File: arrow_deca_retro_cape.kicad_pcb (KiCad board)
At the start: 2 copper layers, 100 x 100 mm, 60 parts, among them J1 DB15_Female_HighDensity, J10 Conn_02x06_Odd_Even, J11 PMOD1, J12 PMOD2, J14 Conn_01x02, J15 Conn_01x03, J16 Conn_01x06, J17 Conn_01x02, J18 Conn_01x03, J19 DINC_MIN_TM_6_1, J2 Conn_01x03, J20 PMOD3, J21 USB3_A, J22 Conn_01x03, J3 Conn_01x06, J4 DB9_Male_MountingHoles, J5 DINC_MIN_TM_6_1, J6 Conn_02x20_Odd_Even, J7 Conn_01x03, J8 P8_Male, J9 P9_Male, U4 LM1117-3.3, U5 LM1117-2.5

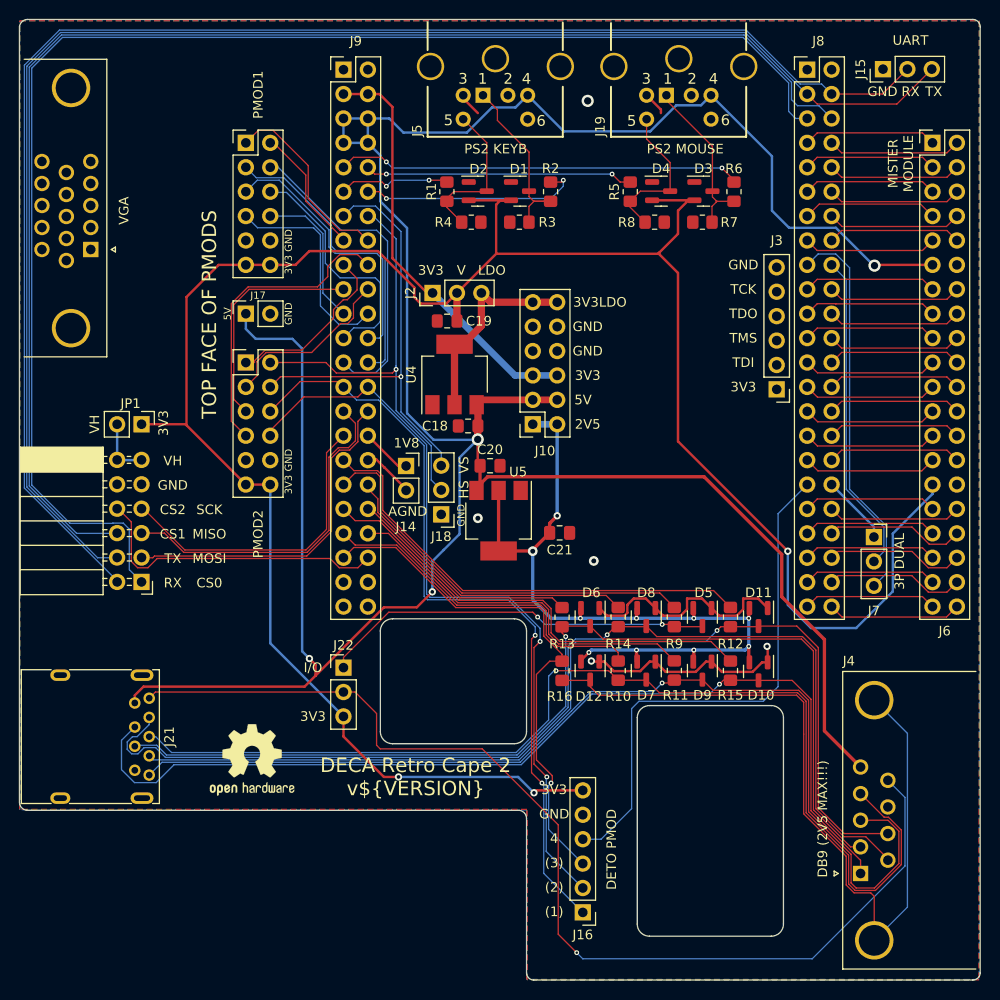
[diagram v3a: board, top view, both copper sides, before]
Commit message: v0.65 power header changed
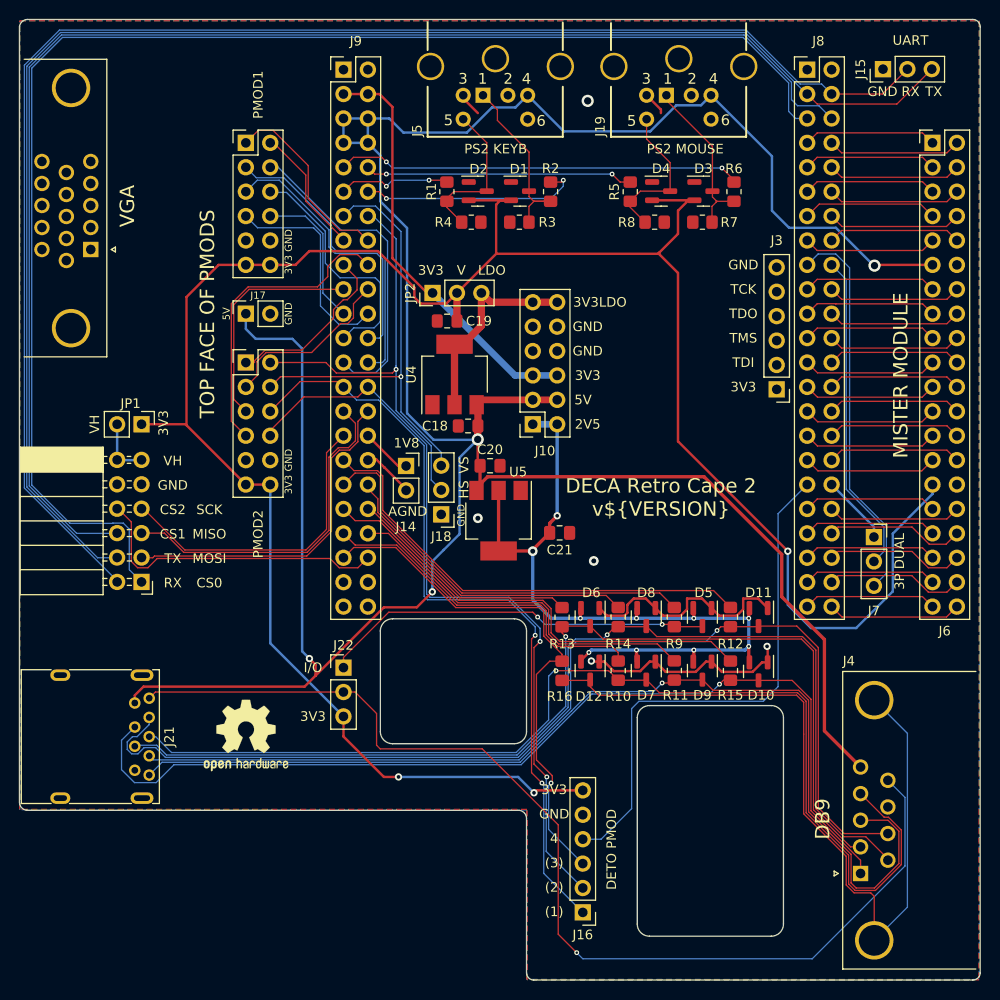
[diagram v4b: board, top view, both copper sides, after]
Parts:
- moved LO2 2.62 mm to (106.7, 114.9)
- renumbered J2 to JP2
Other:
- board text added: "DB9"
- board text removed: "DB9 (2V5 MAX!!!)"
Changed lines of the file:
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@@
     )
   )
-  (property "VERSION" "0.62")
+  (property "VERSION" "0.65")
   (net 0 "")
   (net 1 "GND")
@@
     (property "Sheetname" "")
     (attr through_hole)
-    (fp_text reference "J2" (at 0 -2.33 90) (layer "F.SilkS")
+    (fp_text reference "JP2" (at 0 -2.33 90) (layer "F.SilkS")
       (effects (font (size 1 1) (thickness 0.15)))
     )
@@
   )
   (footprint "Symbol:OSHW-Logo2_9.8x8mm_SilkScreen" (layer "F.Cu")
-    (at 107.315 117.475)
+    (at 106.68 114.935)
     (descr "Open Source Hardware Symbol")
     (tags "Logo Symbol OSHW")
@@
     (effects (font (size 0.75 0.75) (thickness 0.15)))
   )
-  (gr_text "DECA Retro Cape 2\nv${VERSION}" (at 124.333 119.253) (layer "F.SilkS")
+  (gr_text "DECA Retro Cape 2\nv${VERSION}" (at 149.86 90.17) (layer "F.SilkS")
     (effects (font (size 1.5 1.5) (thickness 0.15)))
   )
@@
     (effects (font (size 1 1) (thickness 0.15)))
   )
-  (gr_text "TOP FACE OF PMODS" (at 102.87 71.12 90) (layer "F.SilkS")
+  (gr_text "TOP FACE OF PMODS" (at 102.6668 71.0692 90) (layer "F.SilkS")
     (effects (font (size 1.5 1.5) (thickness 0.15)))
   )
@@
     (effects (font (size 1 1) (thickness 0.15)))
   )
-  (gr_text "DB9 (2V5 MAX!!!)" (at 166.693516 123.623 90) (layer "F.SilkS")
-    (effects (font (size 1 1) (thickness 0.15)))
+  (gr_text "DB9" (at 166.693516 123.623 90) (layer "F.SilkS")
+    (effects (font (size 1.5 1.5) (thickness 0.15)))
   )
   (gr_text "3V3" (at 98.0948 82.423 90) (layer "F.SilkS")
@@
     (effects (font (size 1 1) (thickness 0.15)))
   )
-  (gr_text "MISTER\nMODULE" (at 174.821516 55.424 90) (layer "F.SilkS")
-    (effects (font (size 1 1) (thickness 0.15)))
+  (gr_text "MISTER MODULE" (at 174.821516 77.47 90) (layer "F.SilkS")
+    (effects (font (size 1.5 1.5) (thickness 0.15)))
   )
   (gr_text "VS" (at 129.355516 86.793 90) (layer "F.SilkS")
@@
     (effects (font (size 0.75 0.75) (thickness 0.15)))
   )
-  (gr_text "5V" (at 104.760331 71.045 90) (layer "F.SilkS")
+  (gr_text "5V" (at 104.648 71.045 90) (layer "F.SilkS")
     (effects (font (size 0.75 0.75) (thickness 0.15)))
   )
@@
     (effects (font (size 1 1) (thickness 0.15)))
   )
-  (gr_text "VGA" (at 93.98 60.325 90) (layer "F.SilkS")
-    (effects (font (size 1 1) (thickness 0.15)))
+  (gr_text "VGA" (at 94.3356 59.8424 90) (layer "F.SilkS")
+    (effects (font (size 1.5 1.5) (thickness 0.15)))
   )
   (gr_text "I/O" (at 113.650331 107.875) (layer "F.SilkS")

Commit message: v0.68 vga schematic
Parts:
- added R17: 180, Resistor_SMD:R_0805_2012Metric_Pad1.20x1.40mm_HandSolder, F.Cu at (103.5, 44.5)
- added R18: 180, Resistor_SMD:R_0805_2012Metric_Pad1.20x1.40mm_HandSolder, F.Cu at (103.5, 47.6)
- added R19: 2k, Resistor_SMD:R_0805_2012Metric_Pad1.20x1.40mm_HandSolder, F.Cu at (96.5, 44.5)
- added R20: 2k, Resistor_SMD:R_0805_2012Metric_Pad1.20x1.40mm_HandSolder, F.Cu at (96.5, 46.4)
- added R21: 2k, Resistor_SMD:R_0805_2012Metric_Pad1.20x1.40mm_HandSolder, F.Cu at (96.5, 48.3)
- added R22: 1k, Resistor_SMD:R_0805_2012Metric_Pad1.20x1.40mm_HandSolder, F.Cu at (96.5, 50.2)
- added R23: 1k, Resistor_SMD:R_0805_2012Metric_Pad1.20x1.40mm_HandSolder, F.Cu at (96.5, 52.1)
- added R24: 1k, Resistor_SMD:R_0805_2012Metric_Pad1.20x1.40mm_HandSolder, F.Cu at (96.5, 54.0)
- added R25: 2k, Resistor_SMD:R_0805_2012Metric_Pad1.20x1.40mm_HandSolder, F.Cu at (96.5, 68.6)
- added R26: 2k, Resistor_SMD:R_0805_2012Metric_Pad1.20x1.40mm_HandSolder, F.Cu at (96.5, 70.5)
- added R27: 2k, Resistor_SMD:R_0805_2012Metric_Pad1.20x1.40mm_HandSolder, F.Cu at (96.5, 72.4)
- added R28: 1k, Resistor_SMD:R_0805_2012Metric_Pad1.20x1.40mm_HandSolder, F.Cu at (96.5, 74.3)
- added R29: 1k, Resistor_SMD:R_0805_2012Metric_Pad1.20x1.40mm_HandSolder, F.Cu at (96.5, 76.2)
- added R30: 1k, Resistor_SMD:R_0805_2012Metric_Pad1.20x1.40mm_HandSolder, F.Cu at (96.5, 78.1)
- added R31: 2k, Resistor_SMD:R_0805_2012Metric_Pad1.20x1.40mm_HandSolder, F.Cu at (96.5, 56.5)
- added R32: 2k, Resistor_SMD:R_0805_2012Metric_Pad1.20x1.40mm_HandSolder, F.Cu at (96.5, 58.4)
- added R33: 2k, Resistor_SMD:R_0805_2012Metric_Pad1.20x1.40mm_HandSolder, F.Cu at (96.5, 60.3)
- added R34: 1k, Resistor_SMD:R_0805_2012Metric_Pad1.20x1.40mm_HandSolder, F.Cu at (96.5, 62.2)
- added R35: 1k, Resistor_SMD:R_0805_2012Metric_Pad1.20x1.40mm_HandSolder, F.Cu at (96.5, 64.1)
- added R36: 1k, Resistor_SMD:R_0805_2012Metric_Pad1.20x1.40mm_HandSolder, F.Cu at (96.5, 66.0)
- R1, R10, R11, R12, R13, R14, R15, R16, R2, R9: value 100 -> 180
- R5, R6: value 120 -> 180
- moved JP1 4.36 mm to (91.4, 82.5)
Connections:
- J1 pad 13: VGA222_HS -> Net-(J1-Pad13)
- J1 pad 14: VGA222_VS -> Net-(J1-Pad14)
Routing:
- net +3V3: track 236.6 -> 242.2 mm
- net /VH_PMOD: track 6.58 -> 8.78 mm
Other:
- board text added: "PMOD3"
- board text added: "USER PORT"
- board text added: "created by Hard Team Deca Somhic & Rhoderik & C.Palmero"
- board text removed: "created by Hard Team Deca Somhic & Rhoderik & C.Palmero (PCB adapted from Tom Verbeure)"

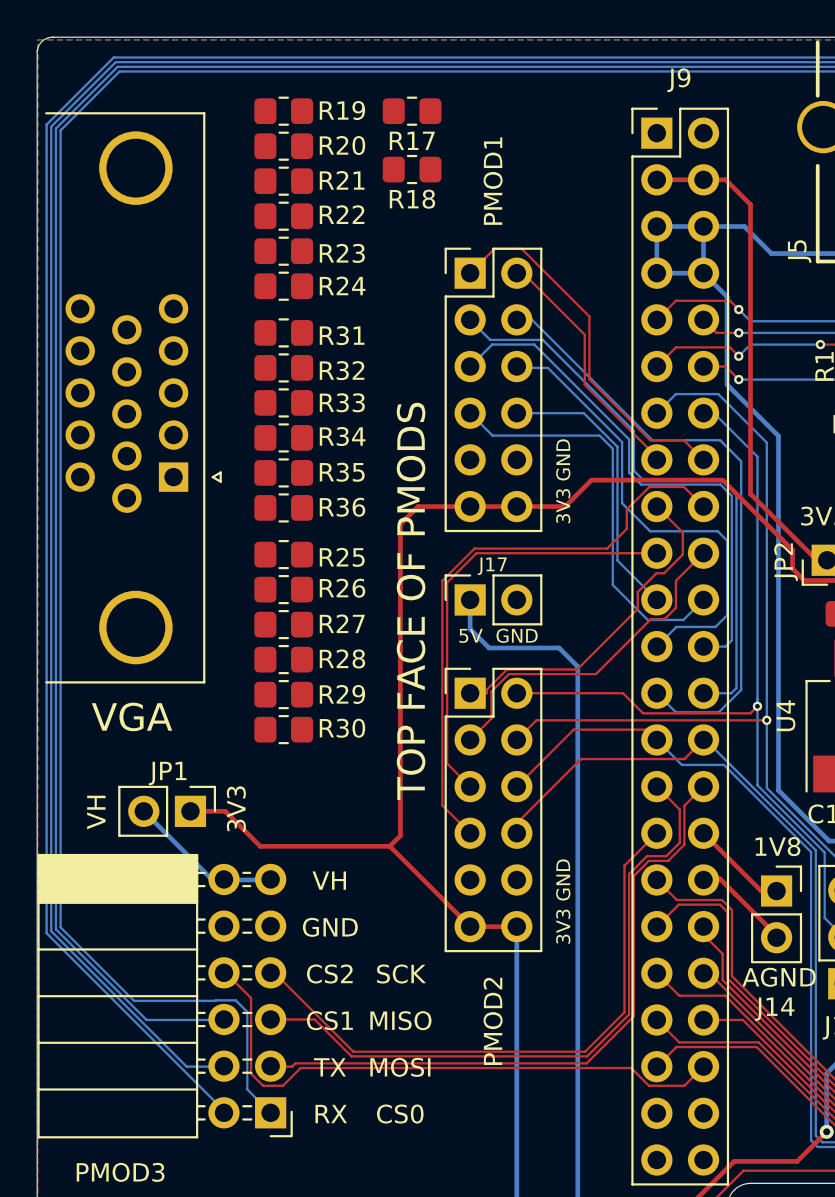
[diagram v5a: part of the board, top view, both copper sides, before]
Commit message: v0.7 routing finished including vga
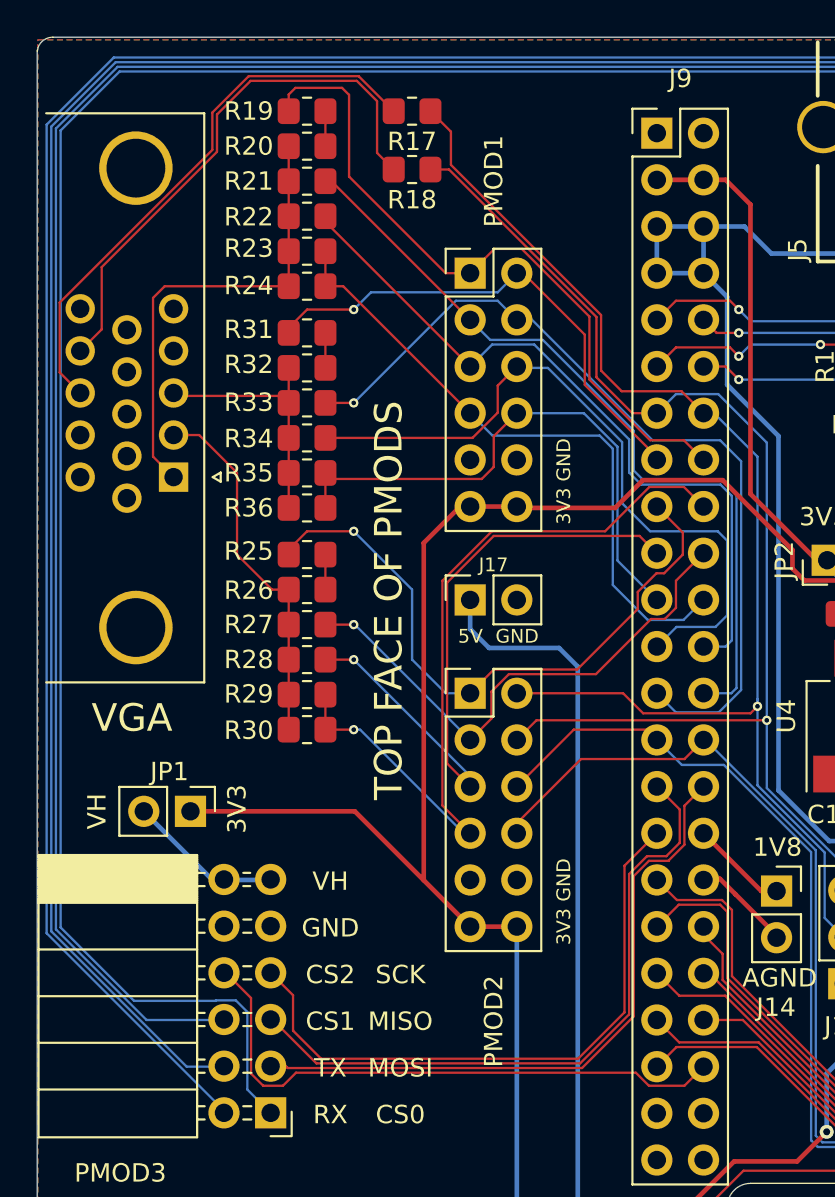
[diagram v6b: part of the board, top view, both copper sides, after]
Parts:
- moved R19 1.27 mm to (97.8, 44.5), turned to 180 degrees
- moved R20 1.27 mm to (97.8, 46.4), turned to 180 degrees
- moved R21 1.27 mm to (97.8, 48.3), turned to 180 degrees
- moved R22 1.27 mm to (97.8, 50.2), turned to 180 degrees
- moved R23 1.27 mm to (97.8, 52.1), turned to 180 degrees
- moved R24 1.27 mm to (97.8, 54.0), turned to 180 degrees
- moved R25 1.27 mm to (97.8, 68.6), turned to 180 degrees
- moved R26 1.27 mm to (97.8, 70.5), turned to 180 degrees
- moved R27 1.27 mm to (97.8, 72.4), turned to 180 degrees
- moved R28 1.27 mm to (97.8, 74.3), turned to 180 degrees
- moved R29 1.27 mm to (97.8, 76.2), turned to 180 degrees
- moved R30 1.27 mm to (97.8, 78.1), turned to 180 degrees
- moved R31 1.27 mm to (97.8, 56.5), turned to 180 degrees
- moved R32 1.27 mm to (97.8, 58.4), turned to 180 degrees
- moved R33 1.27 mm to (97.8, 60.3), turned to 180 degrees
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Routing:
- net Net-(J1-Pad13): track 0.00 -> 30.6 mm
- net Net-(J1-Pad14): track 0.00 -> 30.0 mm
- net /VGAR: track 0.00 -> 25.5 mm
- net /VGA_HS: track 46.1 -> 70.6 mm
- net /VGAG: track 0.00 -> 20.0 mm
- net /VGA_VS: track 47.7 -> 67.4 mm
- net /VGA_R0: track 20.0 -> 37.7 mm
- net /VGA_G0: track 18.6 -> 34.9 mm, vias 0 -> 1
- net /VGA_B3: track 15.5 -> 30.4 mm
- net /VGAB: track 0.00 -> 14.1 mm
- net /VGA_B0: track 13.5 -> 27.4 mm, vias 0 -> 1
- net /VGA_B1: track 33.4 -> 46.6 mm, vias 0 -> 1
- net /VGA_B2: track 25.9 -> 38.8 mm
- net /VGA_R3: track 22.2 -> 34.8 mm
- net /VGA_G2: track 23.7 -> 35.6 mm, vias 0 -> 1
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
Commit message: updated readme and routing improvement
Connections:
- net Net-(J1-Pad13) renamed /VGAHS
- net Net-(J1-Pad14) renamed /VGAVS
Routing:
- net +5V: track 299.3 -> 279.5 mm, vias 4 -> 5
- net +3V3: track 242.0 -> 244.6 mm, vias 3 -> 2
- net /DETO4: track 55.3 -> 54.3 mm
- net /VGAHS: track 30.6 -> 31.4 mm
- net /JOY_MUX_DETO3: track 54.9 -> 55.5 mm
- net GND: vias 5 -> 6

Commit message: update
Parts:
- removed R7, R8: DNI, Resistor_SMD:R_0805_2012Metric_Pad1.20x1.40mm_HandSolder
- C18, C19: footprint Capacitor_SMD:C_0805_2012Metric_Pad1.15x1.40mm_HandSolder -> Capacitor_SMD:C_0805_2012Metric_Pad1.18x1.45mm_HandSolder
- J1: value DB15_Female_HighDensity -> DB15_Female_HighDensity_MountingHoles
- moved C21 8.59 mm to (132.1, 98.5), turned to 180 degrees
- moved J4 2.02 mm to (172.7, 129.4)
- moved C18 0.23 mm to (129.8, 83.0)
- moved J11 0.08 mm to (106.7, 53.3)
- moved J12 0.08 mm to (106.7, 76.2)
- moved J17 0.08 mm to (106.7, 71.1)
- moved J18 0.08 mm to (127.0, 92.0)
- moved JP1 0.08 mm to (91.5, 82.6)
- moved C19 0.08 mm to (127.6, 71.9)
- moved D1 0.08 mm to (135.2, 58.4)
- moved D10 0.08 mm to (160.0, 108.3)
- moved D11 0.08 mm to (160.0, 102.7)
- moved D12 0.08 mm to (142.5, 108.3)
- moved D2 0.08 mm to (130.8, 58.4)
- moved D3 0.08 mm to (154.3, 58.4)
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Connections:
- J1 pad 0: (no net) -> GND
- J4 pad 9: /TX+ -> Net-(D5-Pad3)
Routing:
- net Net-(D5-Pad3): track 41.0 -> 137.0 mm, vias 2 -> 3
- net /TX+: track 112.7 -> 20.5 mm, vias 1 -> 0
- net Net-(D4-Pad3): track 15.9 -> 13.1 mm
- net Net-(D3-Pad3): track 17.4 -> 14.6 mm
- net /TX-: track 113.8 -> 116.0 mm
- net /D+: track 106.1 -> 108.3 mm
- net /D-: track 102.8 -> 105.0 mm
- net /RX+: track 105.2 -> 107.4 mm
- net +2V5: track 84.7 -> 86.5 mm, vias 10 -> 9
- net +5V: track 279.5 -> 281.3 mm
- net /RX-: track 108.5 -> 109.4 mm
- net /DRAIN: track 113.7 -> 114.6 mm
- net /MUX: track 83.3 -> 84.1 mm
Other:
- board text added: "1"
